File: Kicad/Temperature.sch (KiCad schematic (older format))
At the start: 3 parts

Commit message: first pass at layout
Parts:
- removed C3: .1, ~, symbol C
- removed R9: 0K, ~, symbol R
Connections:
- net labels added: GND, Vclean
- net labels removed: AGND, V+_WallWart
- wire segments 9 -> 5
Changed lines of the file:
@@
 $Descr A4 11693 8268
 encoding utf-8
-Sheet 8 8
+Sheet 7 8
 Title ""
-Date "8 dec 2014"
+Date "17 dec 2014"
 Rev ""
 Comp ""
@@
 Wire Notes Line
 	5350 3100 6000 3100
-Text HLabel 1250 1500 0    60   Input ~ 0
-V+_WallWart
-$Comp
-L C C3
-U 1 1 544542CF
-P 1750 1950
-F 0 "C3" H 1750 2050 40  0000 L CNN
-F 1 ".1" H 1756 1865 40  0000 L CNN
-F 2 "~" H 1788 1800 30  0000 C CNN
-F 3 "~" H 1750 1950 60  0000 C CNN
-	1    1750 1950
-	1    0    0    -1
-$EndComp
-Wire Wire Line
-	1750 1750 1750 1500
 Wire Notes Line
 	6000 3300 6500 3300
@@
 Wire Wire Line
 	1250 1500 6500 1500
-Connection ~ 1750 1500
 Wire Wire Line
-	1750 2150 1750 2300
-Wire Wire Line
-	1750 2300 1950 2300
-Text HLabel 2650 3300 0    60   Output ~ 0
-AGND
-Text HLabel 1950 2300 2    60   Output ~ 0
-AGND
-$Comp
-L R R9
-U 1 1 546CA129
-P 4900 3300
-F 0 "R9" V 4980 3300 40  0000 C CNN
-F 1 "0K" V 4907 3301 40  0000 C CNN
-F 2 "~" V 4830 3300 30  0000 C CNN
-F 3 "~" H 4900 3300 30  0000 C CNN
-	1    4900 3300
-	0    -1   -1   0
-$EndComp
-Wire Wire Line
-	5300 3300 5150 3300
-Wire Wire Line
-	3950 3300 4650 3300
+	3950 3300 5300 3300
 Connection ~ 4550 3300
+Text GLabel 1250 1500 0    60   Input ~ 0
+Vclean
+Text GLabel 2650 3300 0    60   Output ~ 0
+GND
 $EndSCHEMATC

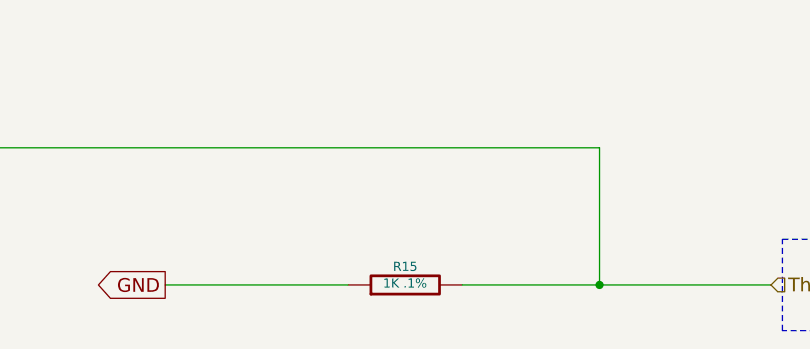
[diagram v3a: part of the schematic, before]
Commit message: changed diodes added test points
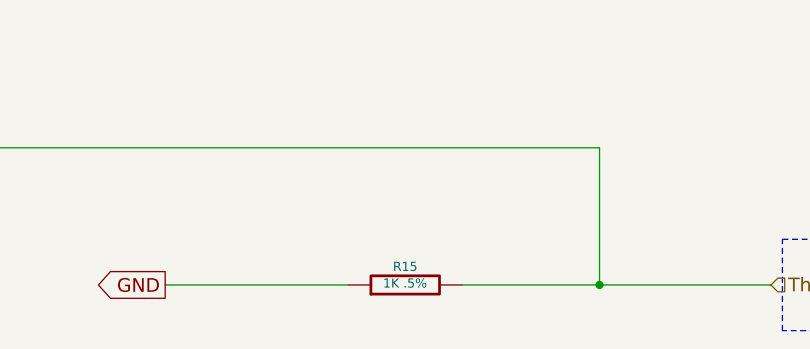
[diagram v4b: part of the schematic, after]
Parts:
- R15: value 1K .1% -> 1K .5%
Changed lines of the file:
@@
 Sheet 7 8
 Title ""
-Date "18 dec 2014"
+Date "20 dec 2014"
 Rev ""
 Comp ""
@@
 P 3700 3300
 F 0 "R15" V 3780 3300 40  0000 C CNN
-F 1 "1K  .1%" V 3707 3301 40  0000 C CNN
+F 1 "1K  .5%" V 3707 3301 40  0000 C CNN
 F 2 "~" V 3630 3300 30  0000 C CNN
 F 3 "~" H 3700 3300 30  0000 C CNN

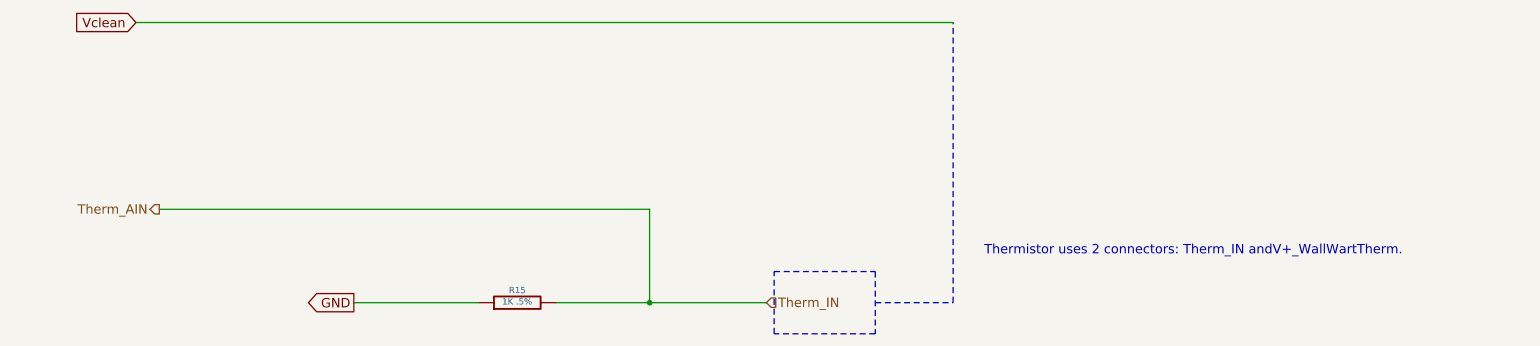
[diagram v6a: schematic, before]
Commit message: Added Thermistor Arduino Sketch.  Changed schematic/layout: label of R15 from 1K to 10K
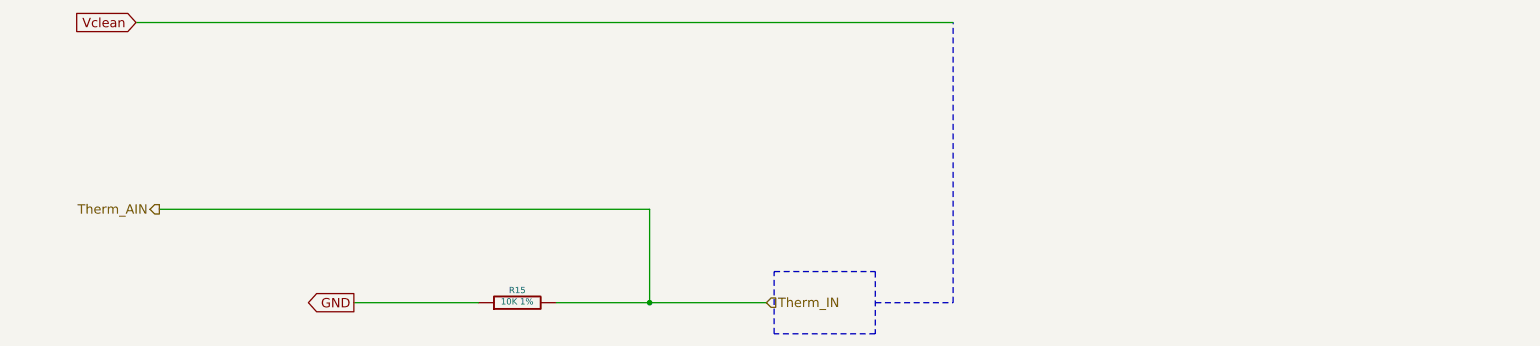
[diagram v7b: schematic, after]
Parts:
- R15: value 1K .5% -> 10K 1%
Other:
- note removed: "Thermistor uses 2 connectors: Therm_IN andV+_WallWartTherm."
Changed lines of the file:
@@
 Sheet 7 8
 Title ""
-Date "27 dec 2014"
+Date "17 jan 2015"
 Rev ""
 Comp ""
@@
 P 3700 3300
 F 0 "R15" V 3780 3300 40  0000 C CNN
-F 1 "1K  .5%" V 3707 3301 40  0000 C CNN
+F 1 "10K 1%" V 3707 3301 40  0000 C CNN
 F 2 "~" V 3630 3300 30  0000 C CNN
 F 3 "~" H 3700 3300 30  0000 C CNN
@@
 Wire Notes Line
 	6500 3300 6500 1500
-Text Notes 6700 3000 0    60   ~ 0
-Thermistor uses 2 connectors: Therm_IN andV+_WallWartTherm.
 Wire Wire Line
 	3450 3300 2650 3300
